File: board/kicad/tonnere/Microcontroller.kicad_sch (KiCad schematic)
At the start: 67 parts, among them J10 STM SWD, J27 I2C, J9 STM GPIO, Q3 2N7002, SW2 USB HS/FS, U11 74LVC1G17, U17 FSUSB42UMX-TP, U20 USB3300-EZK, U21 FSUSB42UMX-TP, U23 STM32F407ZGTx, U26 PCA9546APWR, U4 TPD4E02B04DQA, Y1 24MHz, Y2 8MHz, Y3 32.768KHz

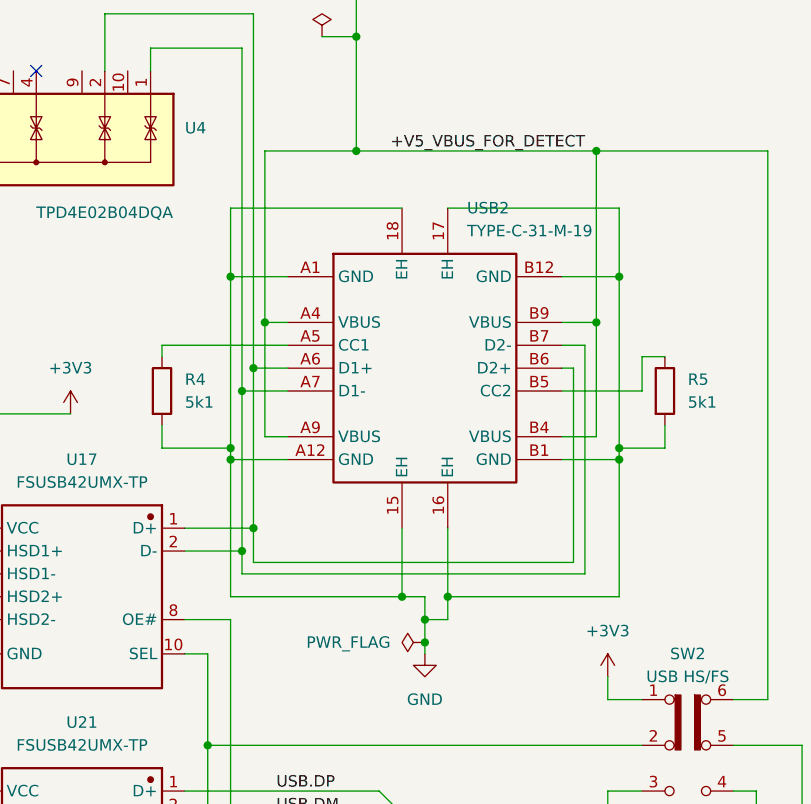
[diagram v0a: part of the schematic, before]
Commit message: Changed USB C flag connector to one with longer pins. JLCPCB did not like the existing one.
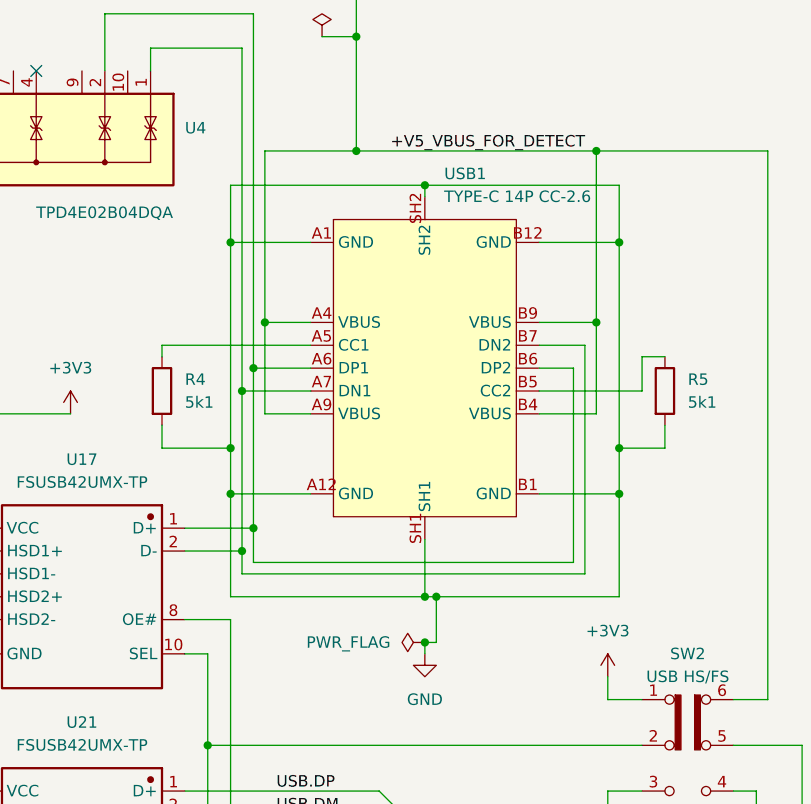
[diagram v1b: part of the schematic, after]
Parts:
- removed USB2: TYPE-C-31-M-19, usb_c_flag:USB-C-TH_TYPE-C-31-M-19, symbol usb_c_flag:TYPE-C-31-M-19
- added USB1: TYPE-C 14P CC-2.6, tonnere:TYPE-C-TH_TYPE-C-14P-CC-2.6, symbol tonnere:TYPE-C14PCC-2.6
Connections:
- net +V5_VBUS_FOR_DETECT: now also USB1.A4 (VBUS), USB1.A9 (VBUS), USB1.B4 (VBUS), USB1.B9 (VBUS)
- net GND: now also USB1.A1 (GND), USB1.A12 (GND), USB1.B1 (GND), USB1.B12 (GND), USB1.SH1, USB1.SH2
- net at U17.2 (D-), U4.1 (IO1): now also USB1.A7 (DN1), USB1.B7 (DN2)
- net at U17.1 (D+), U4.2 (IO2): now also USB1.A6 (DP1), USB1.B6 (DP2)
- net at R4.1: now also USB1.A5 (CC1)
- net at R5.1: now also USB1.B5 (CC2)

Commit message: Moved ADC pins around in order to have a dummy rank to stop bleed at high frequency sampling
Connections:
- net GND: now also U23.36 (PA2)
- net STM.I2CRESET: now also U23.49 (PF11); no longer U23.45 (PC5)
- net STMAUD.ADC.L: now also U23.42 (PA6); no longer U23.36 (PA2)
- net STMAUD.ADC.PBI: now also U23.44 (PC4); no longer U23.42 (PA6)
- net STMAUD.ADC.SIO: now also U23.45 (PC5); no longer U23.44 (PC4)
- net at J9.3 (Pin_3): no longer U23.49 (PF11)
- no-connect marks 5 -> 6
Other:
- note added: "ADCDUMMY"

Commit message: Changed video dac to 5 bit R2R and 6th-8th bits as pattern and/or sigma delta.
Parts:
- renumbered C10 to C11, C15 to C16, C16 to C17, C17 to C18, C18 to C19, C20 to C21, C21 to C22, C22 to C23, C24 to C25, C25 to C26, C28 to C29, C30 to C31, C32 to C33, C34 to C35, C35 to C36, C36 to C37, C40 to C41, C44 to C45, C49 to C50, C52 to C54, C55 to C58, C57 to C63, C60 to C66, C63 to C67, C64 to C68, C66 to C70, J27 to J26, J9 to J8, J10 to J9, R51 to R54, R53 to R56, R54 to R57, R55 to R58, R57 to R60, R60 to R63, R61 to R64, R62 to R68, R63 to R69, R9 to R8, R77 to R84, R78 to R85, U11 to U12, U17 to U18, U20 to U21, U21 to U22, U23 to U25, U26 to U27, U4 to U5, USB1 to USB2
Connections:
- net Net-(J10-Pin_2): now reaches J9.2 (Pin_2), U25.105 (PA13)
- net Net-(J10-Pin_3): now reaches J9.3 (Pin_3), U25.109 (PA14)
- net Net-(J27-Pin_4): now reaches J26.4 (Pin_4), U27.6 (SD1)
- net Net-(J27-Pin_3): now reaches J26.3 (Pin_3), U27.7 (SC1)
- net Net-(USB1-CC1): now reaches R4.1, USB2.A5 (CC1)
- net Net-(U17-D+): now reaches U18.1 (D+), U5.2 (IO2), USB2.A6 (DP1), USB2.B6 (DP2)
- net Net-(U17-D-): now reaches U18.2 (D-), U5.1 (IO1), USB2.A7 (DN1), USB2.B7 (DN2)
- net Net-(USB1-CC2): now reaches R5.1, USB2.B5 (CC2)
- net Net-(U20-XI): now reaches C19.2, R37.2, U21.28 (XI), Y1.1
- net Net-(U20-XO): now reaches C16.2, R37.1, U21.27 (XO), Y1.3
- net unconnected-(U4-NC-Pad10): now reaches U5.10 (NC)
- net unconnected-(U4-IO3-Pad4): now reaches U5.4 (IO3)
- net unconnected-(U4-IO4-Pad5): now reaches U5.5 (IO4)
- net unconnected-(U4-NC-Pad6): now reaches U5.6 (NC)
- net unconnected-(U4-NC-Pad7): now reaches U5.7 (NC)
- net unconnected-(U4-NC-Pad9): now reaches U5.9 (NC)
- net Net-(U23-PB3): now reaches R64.1, U25.133 (PB3)
- net Net-(U17-SEL): now reaches SW2.2 (B), U18.10 (SEL), U22.10 (SEL)
- net Net-(C49-Pad1): now reaches C50.1, R56.2, SW2.5 (B)
- net Net-(U23-PH0): now reaches C18.2, R39.1, U25.23 (PH0), Y2.3
- net Net-(U23-PA11): now reaches R84.1, U25.103 (PA11)
- net Net-(U23-PC15): now reaches C25.2, U25.9 (PC15), Y3.2
- net Net-(J9-Pin_7): now reaches J8.7 (Pin_7), U25.1 (PE2)
- net Net-(U23-PA12): now reaches R85.1, U25.104 (PA12)
- net Net-(U23-VCAP_2): now reaches C67.1, U25.106 (VCAP_2)
- net Net-(J9-Pin_6): now reaches J8.6 (Pin_6), U25.110 (PA15)
- net Net-(U23-PH1): now reaches C17.2, R39.2, U25.24 (PH1), Y2.1
- net Net-(U23-VCAP_1): now reaches C66.1, U25.71 (VCAP_1)
- net Net-(J9-Pin_4): now reaches J8.4 (Pin_4), U25.75 (PB14)
- net Net-(J9-Pin_5): now reaches J8.5 (Pin_5), U25.76 (PB15)
- net Net-(U23-PC14): now reaches C26.2, U25.8 (PC14), Y3.1
- net Net-(U20-RBIAS): now reaches R42.1, U21.32 (RBIAS)
- net Net-(U20-VBUS): now reaches R56.1, U21.4 (VBUS)
- net unconnected-(J9-Pin_3-Pad3): now reaches J8.3 (Pin_3)
- net unconnected-(U20-EXTVBUS-Pad10): now reaches U21.10 (EXTVBUS)
- net unconnected-(U20-CPEN-Pad3): now reaches U21.3 (CPEN)
- net unconnected-(U20-ID-Pad5): now reaches U21.5 (ID)
- net Net-(U20-RESET): now reaches R60.1, U21.9 (RESET)
- net Net-(C20-Pad1): now reaches C21.1, R57.1, U12.4
- net unconnected-(U11-NC-Pad1): now reaches U12.1 (NC)
